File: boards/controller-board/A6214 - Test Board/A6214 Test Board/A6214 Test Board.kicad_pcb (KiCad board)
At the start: 2 copper layers, 54 x 44.3 mm, 30 parts, among them IC1 A6214KLKTR-T, J1 Conn_01x02, J2 Conn_01x02, J3 Conn_01x02, J4 1995499, J5 1995499

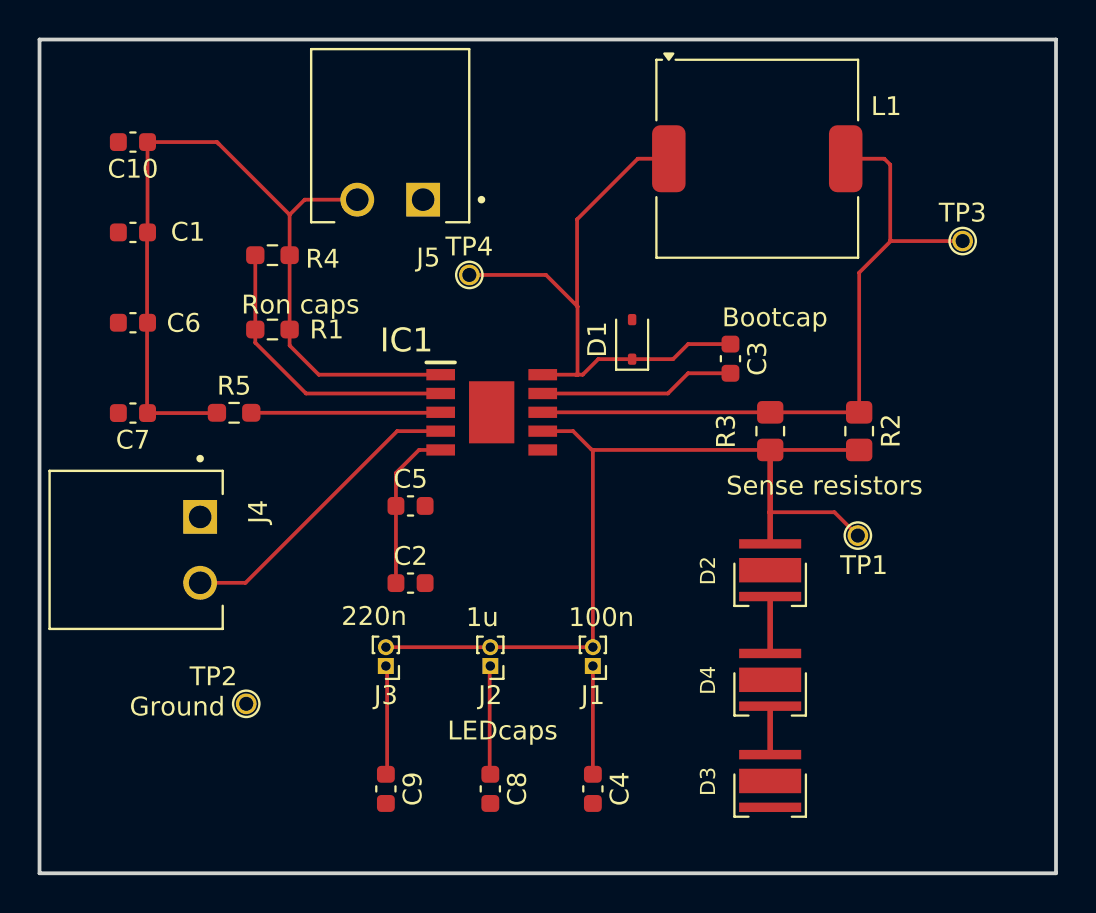
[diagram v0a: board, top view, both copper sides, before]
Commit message: finished test board for A6214 and created files for printing
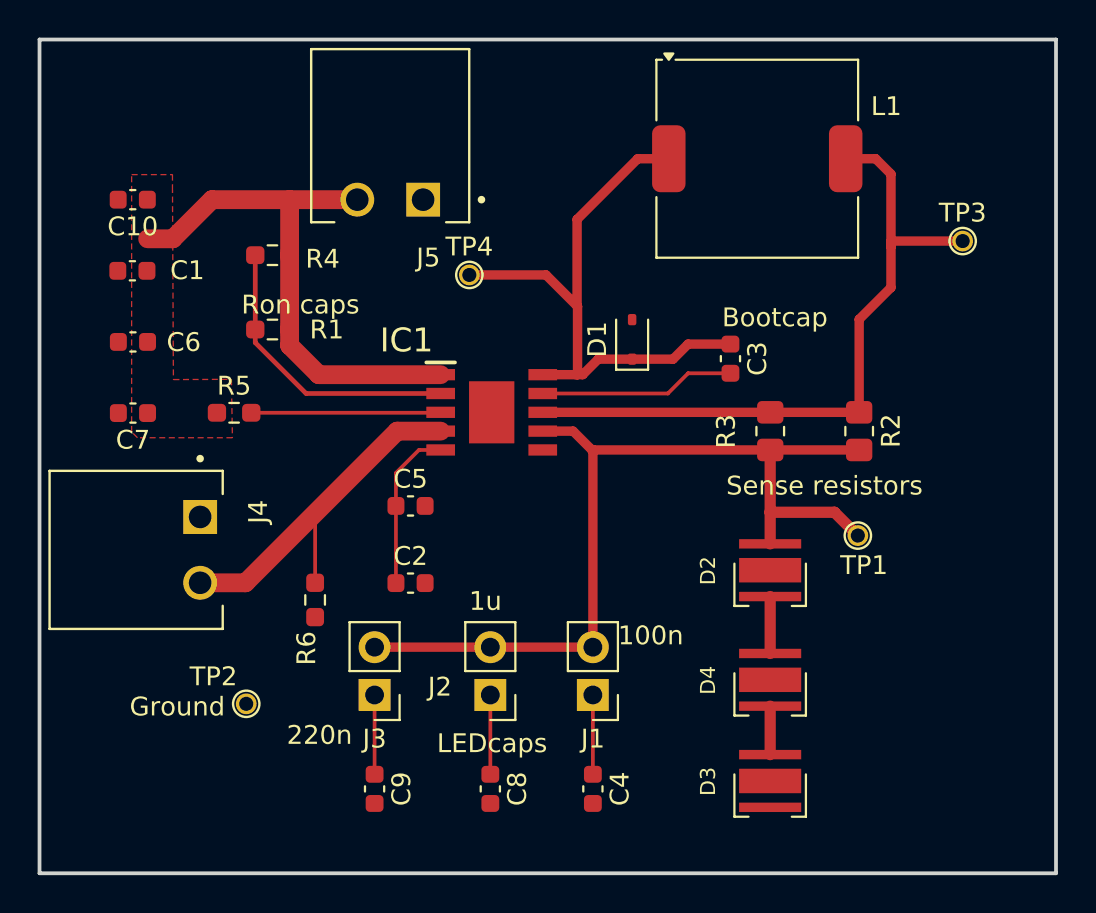
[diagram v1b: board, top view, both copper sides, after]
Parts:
- added R6: 10k, Resistor_SMD:R_0603_1608Metric_Pad0.98x0.95mm_HandSolder, F.Cu at (140.7, 104.6)
- J1, J2, J3: footprint Connector_PinHeader_1.00mm:PinHeader_1x02_P1.00mm_Vertical -> Connector_PinHeader_2.54mm:PinHeader_1x02_P2.54mm_Vertical
- moved C10 3.06 mm to (131.0, 83.3)
- moved C1 2.04 mm to (131.0, 87.1)
- moved J3 1.65 mm to (143.9, 109.7)
- moved J1 1.54 mm to (155.5, 109.7)
- moved J2 1.54 mm to (150.0, 109.7)
- moved C6 1.02 mm to (131.1, 90.9)
- moved C9 0.60 mm to (143.9, 114.7)
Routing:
- net Net-(IC1-VIN): track 46.9 -> 28.4 mm
- net Net-(IC1-ADIM): track 16.1 -> 26.0 mm
- net Net-(J3-Pin_1): track 5.78 -> 4.22 mm
- net Net-(J2-Pin_1): track 5.77 -> 4.22 mm
- net Net-(J1-Pin_1): track 5.76 -> 4.22 mm
- added copper zone on F.Cu, net Net-(IC1-VIN)
